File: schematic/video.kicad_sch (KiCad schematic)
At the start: 15 parts, among them J1 Conn_Coaxial, J8 SJ1-3525NG, Q1 2N3904, U1 TMS4416, U14 TMS9118NL, U3 TMS4416, Y1 Crystal

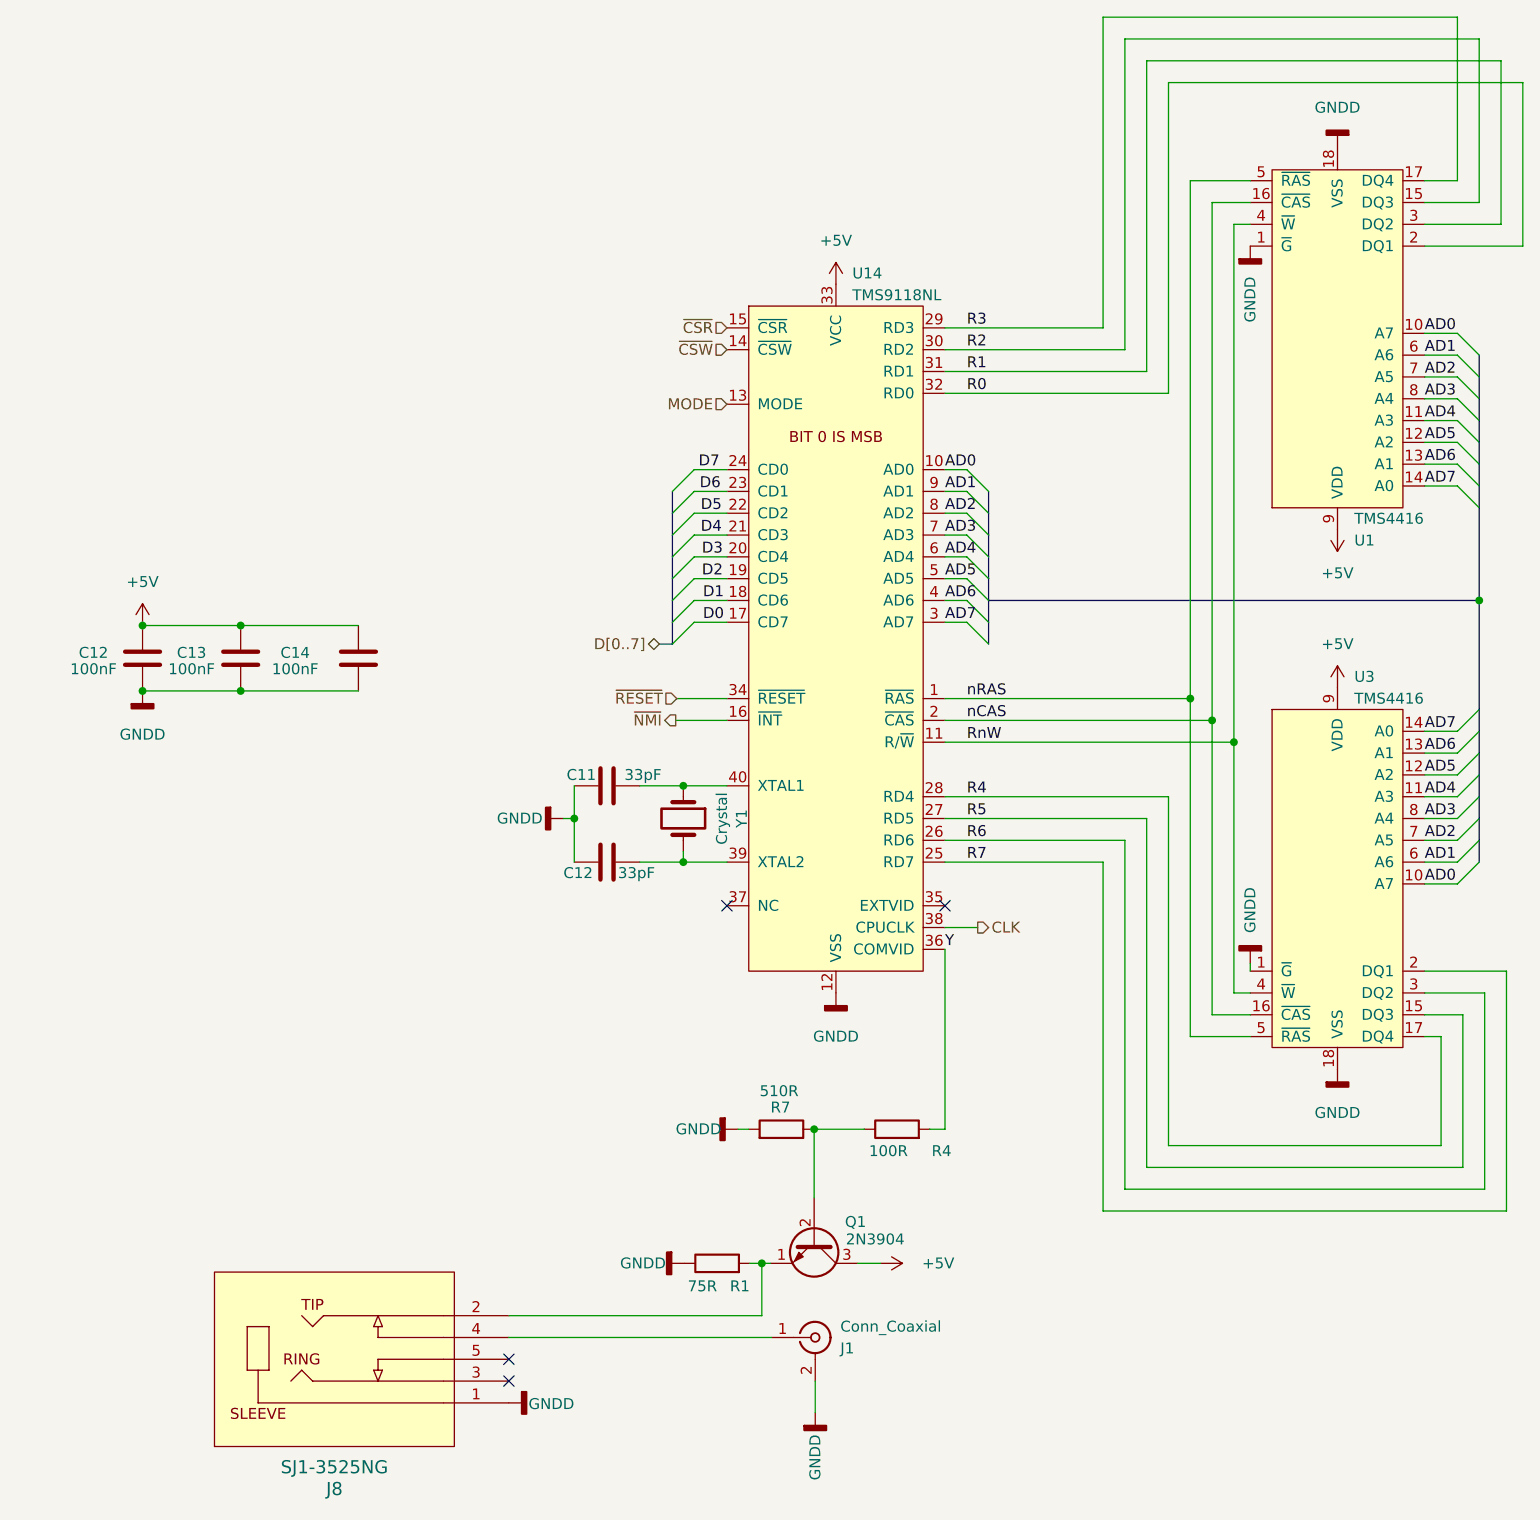
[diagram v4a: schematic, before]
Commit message: added filtering to the video circuit. Idea is to to keep the video and audio circuits as clean and seperated as possible for the power rails.
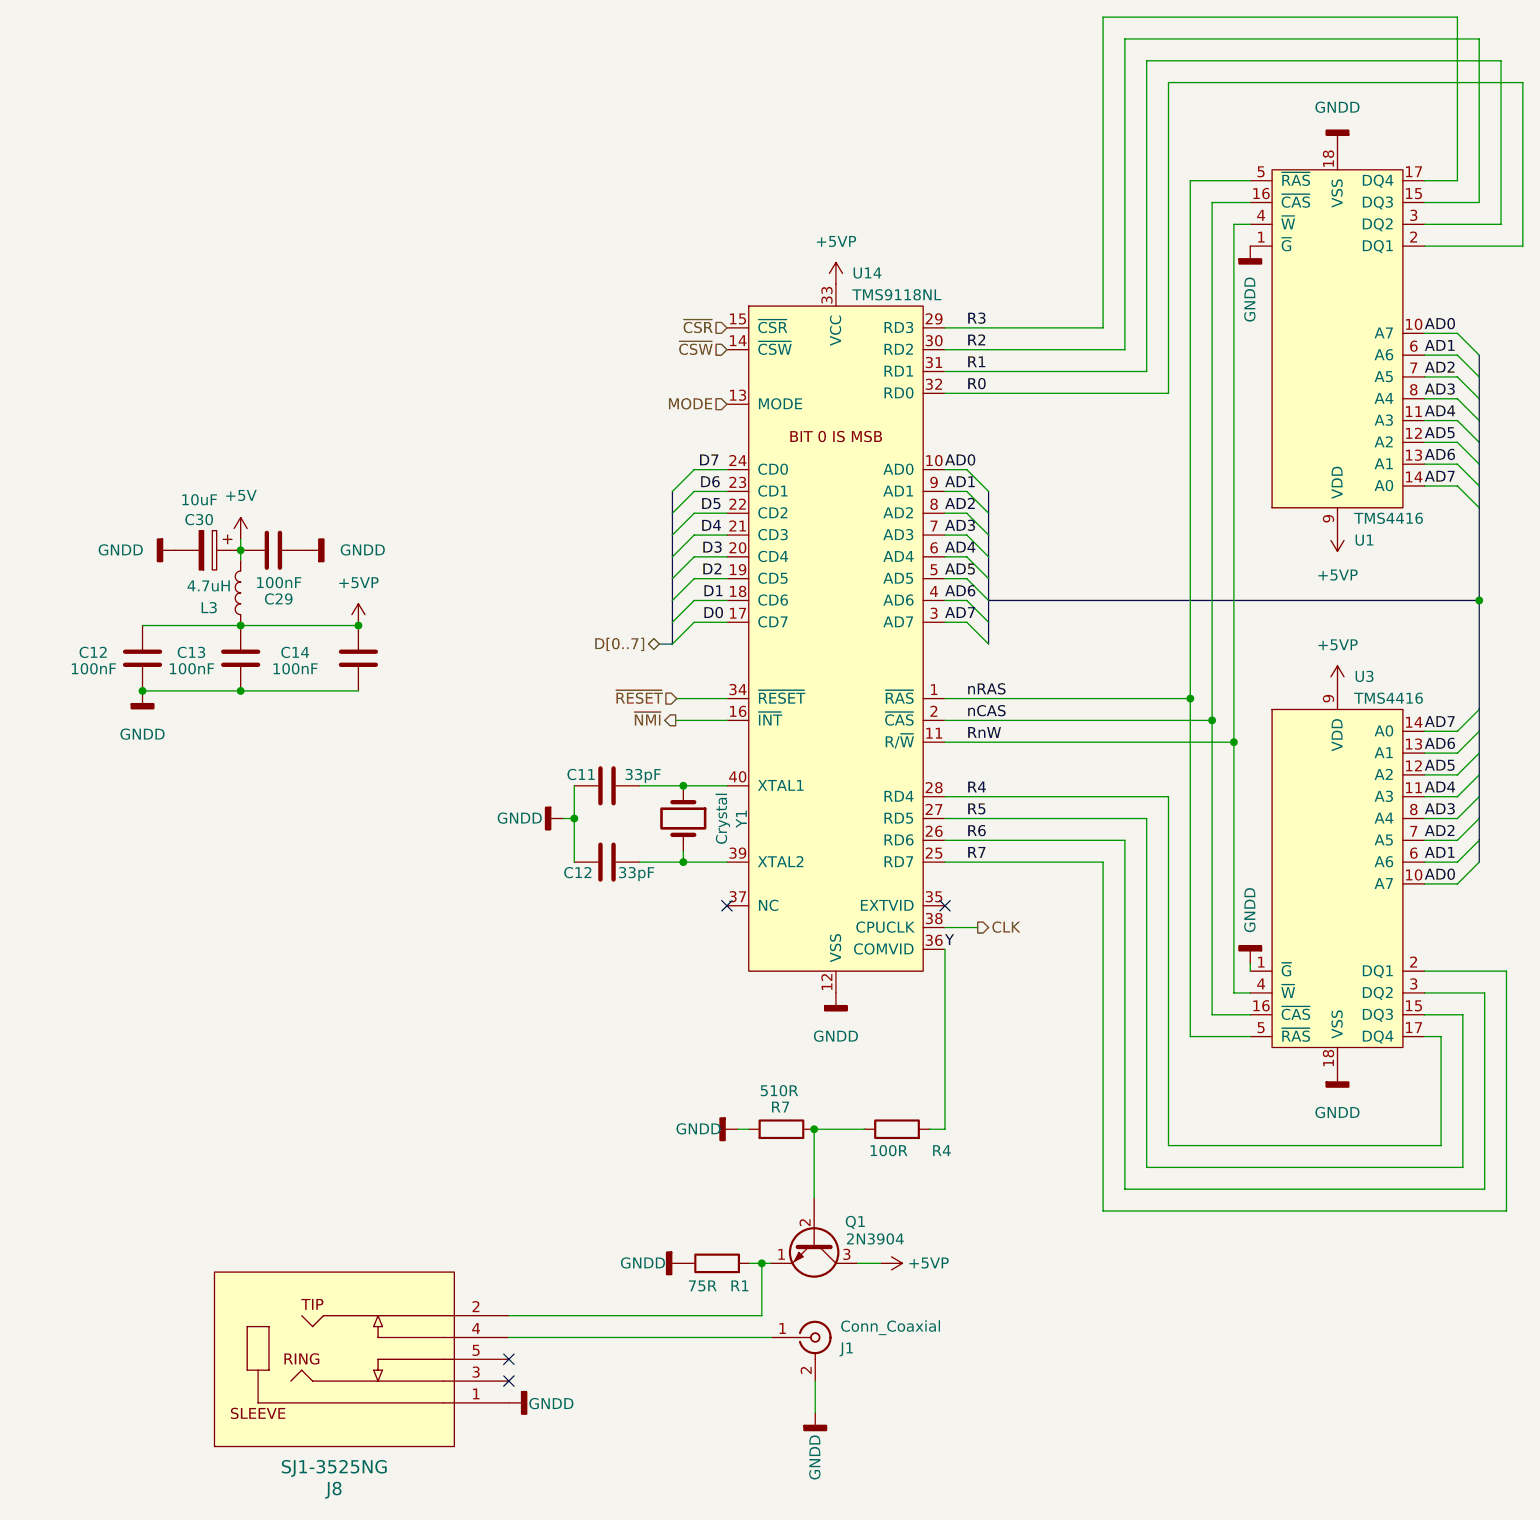
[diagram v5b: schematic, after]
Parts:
- added C29: 100nF, Capacitor_THT:C_Disc_D7.0mm_W2.5mm_P5.00mm, symbol Device:C
- added C30: 10uF, Capacitor_THT:CP_Radial_D5.0mm_P2.50mm, symbol Device:CP
- added L3: 4.7uH, Inductor_THT:L_Axial_L7.0mm_D3.3mm_P10.16mm_Horizontal_Fastron_MICC, symbol Device:L
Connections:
- net +5V: now also C29.1, C30.1, L3.2; no longer C12.1, C13.1, C14.1, Q1.3 (C), U1.9 (VDD), U14.33 (VCC), U3.9 (VDD)
- net GNDD: now also C29.2, C30.2
- new net +5VP: C12.1, C13.1, C14.1, L3.1, Q1.3 (C), U1.9 (VDD), U14.33 (VCC), U3.9 (VDD)

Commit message: update for release, correct documents, and update readme
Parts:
- Y1: value Crystal -> 10.738635 MHz
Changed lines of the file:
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@@
       (effects (font (size 1.27 1.27)))
     )
-    (property "Value" "Crystal" (at 110.0328 112.522 0)
+    (property "Value" "10.738635 MHz" (at 105.537 126.492 0)
       (effects (font (size 1.27 1.27)))
     )

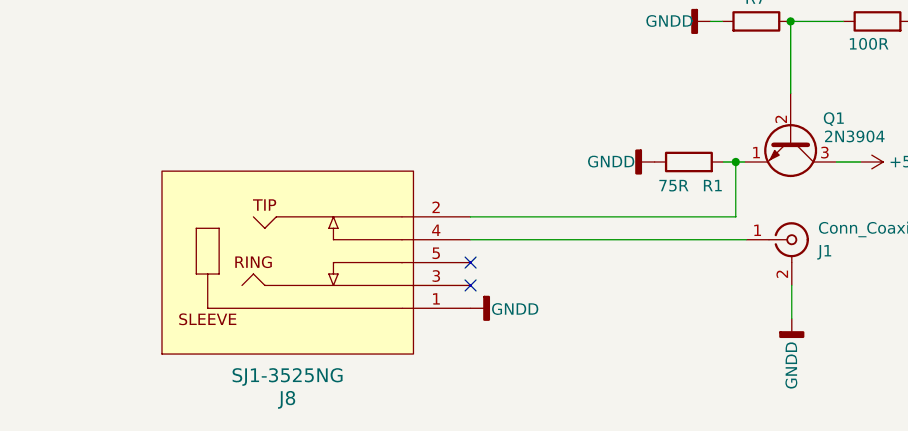
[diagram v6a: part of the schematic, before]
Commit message: schematic updates to remove unused video port
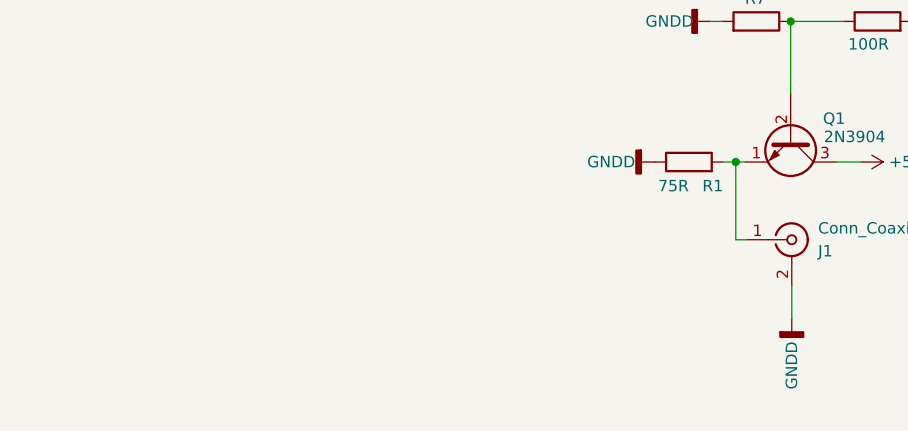
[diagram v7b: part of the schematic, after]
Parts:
- removed J8: SJ1-3525NG, jacks2:SJ1-3525NG_CUD, symbol SJ-63053A:SJ1-3525NG
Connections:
- net at Q1.1 (E), R1.2: now also J1.1 (In)
- no-connect marks 4 -> 2
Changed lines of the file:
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@@
   (junction (at 198.247 87.122) (diameter 0) (color 0 0 0 0)
   )
-  (no_connect (at 85.217 175.514))
   (no_connect (at 136.017 122.682))
   (no_connect (at 110.617 122.682))
-  (no_connect (at 85.217 178.054))
   (bus_entry (at 195.707 104.902) (size 2.54 -2.54)
     (stroke (width 0) (type default))
@@
     (stroke (width 0) (type default))
   )
-  (wire (pts (xy 114.681 164.338) (xy 114.681 170.434))
+  (wire (pts (xy 114.681 164.338) (xy 114.681 172.974))
     (stroke (width 0) (type default))
   )
@@
     (stroke (width 0) (type default))
   )
+  (wire (pts (xy 114.681 172.974) (xy 115.824 172.974))
+    (stroke (width 0) (type default))
+  )
   (wire (pts (xy 106.807 89.662) (xy 110.617 89.662))
     (stroke (width 0) (type default))
@@
     (stroke (width 0) (type default))
   )
-  (wire (pts (xy 85.217 170.434) (xy 114.681 170.434))
-    (stroke (width 0) (type default))
-  )
   (wire (pts (xy 193.802 150.622) (xy 193.802 137.922))
     (stroke (width 0) (type default))
@@
   )
   (wire (pts (xy 191.897 112.522) (xy 195.707 112.522))
-    (stroke (width 0) (type default))
-  )
-  (wire (pts (xy 85.217 172.974) (xy 115.824 172.974))
     (stroke (width 0) (type default))
   )
@@
     )
   )
-  (symbol (lib_id "power:GNDD") (at 85.217 180.594 90) (mirror x) (unit 1)
-    (in_bom yes) (on_board yes) (dnp no)
-    (property "Reference" "#PWR085" (at 91.567 180.594 0)
-      (effects (font (size 1.27 1.27)) hide)
-    )
-    (property "Value" "GNDD" (at 87.503 180.721 90)
-      (effects (font (size 1.27 1.27)) (justify right))
-    )
-    (property "Footprint" "" (at 85.217 180.594 0)
-      (effects (font (size 1.27 1.27)) hide)
-    )
-    (property "Datasheet" "" (at 85.217 180.594 0)
-      (effects (font (size 1.27 1.27)) hide)
-    )
-    (pin "1")
-    (instances
-      (project "coleco_original"
-        (path "/970e0f64-111f-41e3-9f5a-fb0d0f6fa101/00000000-0000-0000-0000-00006262475e"
-          (reference "#PWR085") (unit 1)
-        )
-      )
-    )
-  )
   (symbol (lib_id "Device:R") (at 109.474 164.338 90) (unit 1)
     (in_bom yes) (on_board yes) (dnp no)
@@
         )
       )
-    )
-  )
-  (symbol (lib_id "SJ-63053A:SJ1-3525NG") (at 85.217 180.594 0) (mirror x) (unit 1)
-    (in_bom yes) (on_board yes) (dnp no) (fields_autoplaced)
-    (property "Reference" "J8" (at 64.897 190.627 0)
-      (effects (font (size 1.524 1.524)))
-    )
-    (property "Value" "SJ1-3525NG" (at 64.897 188.087 0)
-      (effects (font (size 1.524 1.524)))
-    )
-    (property "Footprint" "jacks2:SJ1-3525NG_CUD" (at 85.217 180.594 0)
-      (effects (font (size 1.27 1.27) italic) hide)
-    )
-    (property "Datasheet" "SJ1-3525NG" (at 85.217 180.594 0)
-      (effects (font (size 1.27 1.27) italic) hide)
-    )
-    (pin "2")
-    (pin "3")
-    (pin "5")
-    (pin "4")
-    (pin "1")
-    (instances
-      (project "coleco_original"
-        (path "/970e0f64-111f-41e3-9f5a-fb0d0f6fa101/00000000-0000-0000-0000-00006262475e"
-          (reference "J8") (unit 1)
-        )
-      )
